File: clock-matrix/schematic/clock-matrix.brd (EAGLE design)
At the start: 30 x 50 mm, 80 parts, among them IC1 WS2811-SOP8, IC2 WS2811-SOP8, IC3 74HC595D, U1 Tiny45-20-SMT, X2 USB-MICROB

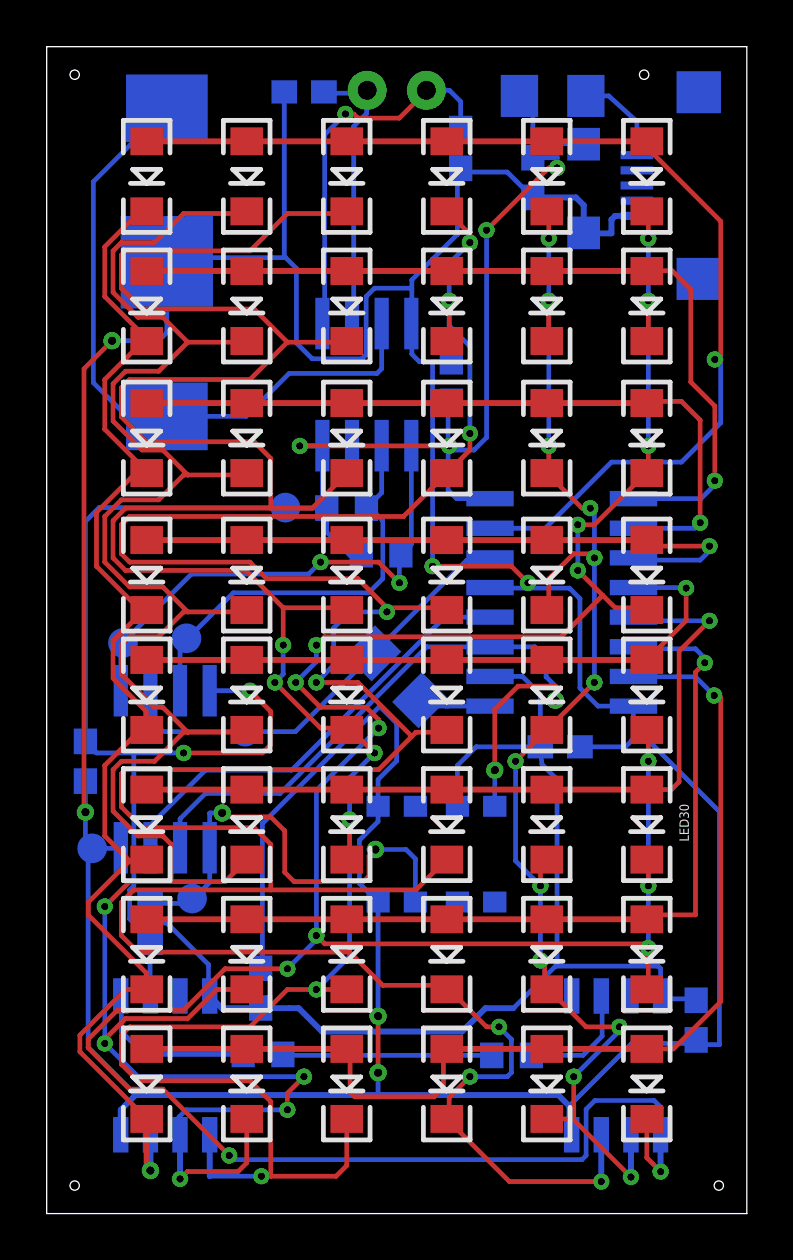
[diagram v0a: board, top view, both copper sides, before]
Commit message: Relocated files, removed unused files, updated christmas and clock board and other changes
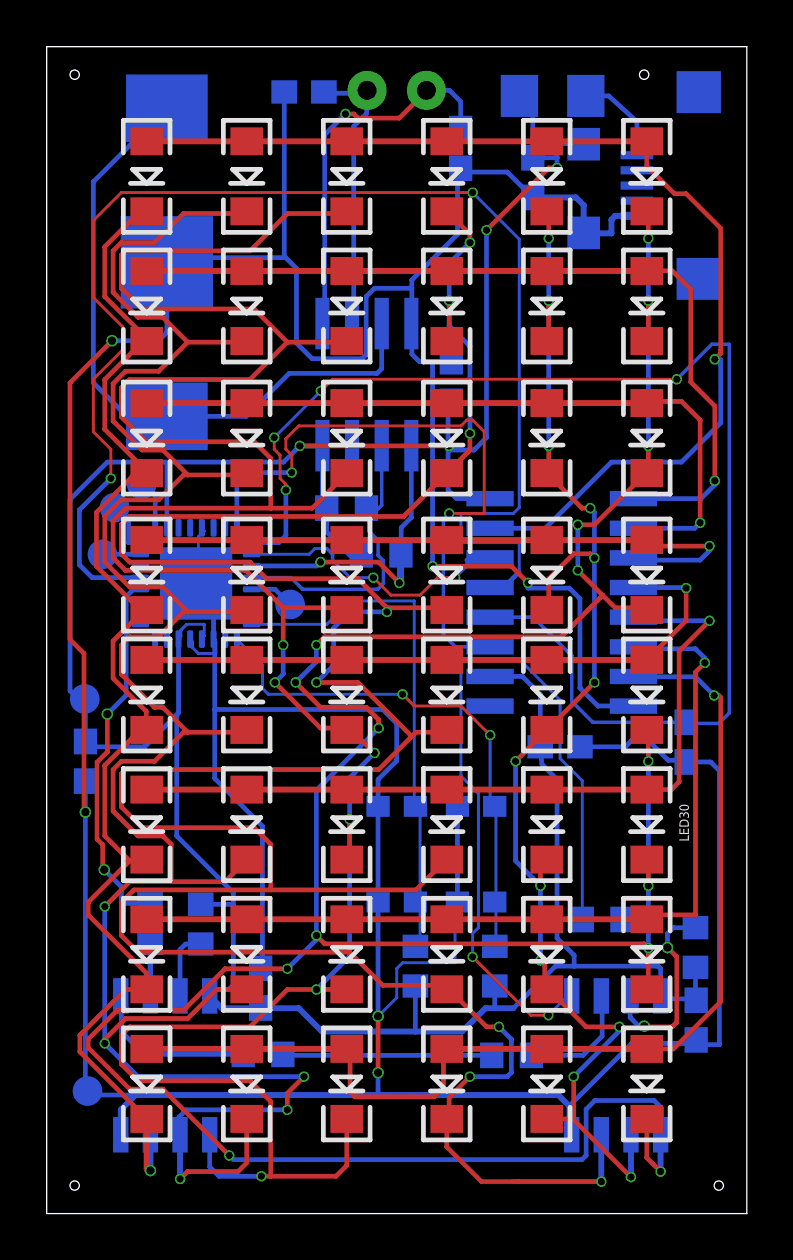
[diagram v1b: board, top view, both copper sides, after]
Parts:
- removed U1: Tiny45-20-SMT, SparkFun-Retired:SO08-EIAJ_MCU
- added C6: (no value), rcl:C0603
- added R2, R4, R7, R8: 33, adafruit:R0603
- added U2: ATMEGA328P-MU, Microcontroller:VQFN-32
- R3: value 0 -> 33; device audio amplifier example:R1206 -> adafruit:R0603
- moved TP1 13.3 mm to (10.4, 26.1)
- moved R3 13.1 mm to (19.2, 10.6), turned to 270 degrees
- moved TP6 11.9 mm to (1.63, 22.1)
- moved TP2 11.1 mm to (2.91, 30.2)
- moved TP5 10.4 mm to (1.75, 5.25)
- moved TP4 6.85 mm to (4.07, 31.2)
- moved TP3 5.09 mm to (2.39, 28.2)
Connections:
- removed net CLK: IC3.11, S1.1, S1.2, U1.2
- removed net RCK: IC3.12, U1.3
- new net AREF: U2.20
- new net BT0: R2.1, S2.1, S2.2, U2.32
- new net BT1: R3.1, S1.1, S1.2, U2.1
- new net LATCH: C6.1, IC3.12, U2.25
- new net LEDDATA: R9.1, U2.12
- new net MISO: TP2.TP, U2.16
- new net MOSI: TP3.TP, U2.15
- new net N$13: IC2.7, R8.2
- new net N$4: IC1.7, R7.2
- new net N$6: U2.8
- new net N$8: U2.7
- new net PWM: IC3.13, U2.13
- new net RCLK: IC3.11, U2.24
- new net RX: U2.30
- new net SCK: TP4.TP, U2.17
- new net TX: U2.31
- net 5V: now also R2.2, R3.2, R7.1, R8.1, U2.18, U2.4, U2.6; no longer S1.3, S1.4, U1.8
- net GND: now also C6.2, S1.3, S1.4, U2.21, U2.3, U2.33, U2.5; no longer IC3.13, U1.4
- net N$5: now also IC2.5, R4.2; no longer IC3.9, R3.1
- net RES: now also U2.29; no longer R9.1, S2.1, S2.2, U1.1
- net SCL: now also U2.28; no longer TP3.TP, U1.7
- net SDA: now also U2.27; no longer TP4.TP, U1.5
- net SER: now also U2.26; no longer R3.2, TP2.TP, U1.6
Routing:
- net PWM: track 0.00 -> 59.7 mm, vias 0 -> 2
- net LATCH: track 0.00 -> 56.4 mm, vias 0 -> 4
- net N$5: track 3.09 -> 33.5 mm, vias 0 -> 2
- net CLK: track 29.9 -> 0.00 mm, vias 2 -> 0
- net RCLK: track 0.00 -> 27.6 mm, vias 0 -> 2
- net GND: track 191.9 -> 217.5 mm
- net BT0: track 0.00 -> 22.7 mm
- net BT1: track 0.00 -> 22.4 mm, vias 0 -> 2
- net RCK: track 19.2 -> 0.00 mm
- net RES: track 20.5 -> 1.91 mm, vias 2 -> 0
- net LEDDATA: track 0.00 -> 16.0 mm, vias 0 -> 2
- net N$13: track 0.00 -> 8.46 mm, vias 0 -> 2
- net SDA: track 22.0 -> 14.4 mm
- net SER: track 20.5 -> 13.1 mm, vias 0 -> 2
- net SCL: track 18.3 -> 13.3 mm
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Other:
- board text removed: "G"
- board text removed: "MI"
- board text removed: "MO"
- board text removed: "R"
- board text removed: "SK"

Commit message: Minor board fixes and other changes
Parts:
- moved R15 0.20 mm to (12.8, 30.4)
- moved TP6 0.20 mm to (1.63, 22.2)
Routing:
- net SDA: track 14.4 -> 13.3 mm
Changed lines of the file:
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@@
 <drawing>
 <settings>
-<setting alwaysvectorfont="no"/>
+<setting alwaysvectorfont="yes"/>
 <setting verticaltext="up"/>
 </settings>
@@
 </class>
 </classes>
-<designrules name="jlcpcb-2layers">
+<designrules name="jlcpcb-2layers *">
 <description language="en">&lt;b&gt;JLCPCB design rules (2 layers)&lt;/b&gt;
 &lt;ul&gt;
@@
 <param name="mlMinCreamFrame" value="0mil"/>
 <param name="mlMaxCreamFrame" value="0mil"/>
-<param name="mlViaStopLimit" value="0mil"/>
+<param name="mlViaStopLimit" value="14mil"/>
 <param name="srRoundness" value="0"/>
 <param name="srMinRoundness" value="0mil"/>
@@
 <attribute name="NAME" x="12.695" y="27.195" size="1.27" layer="26" rot="MR180"/>
 </element>
-<element name="R15" library="rcl" package="R0603" value="10K" x="12.85" y="30.23" smashed="yes" rot="MR180">
-<attribute name="NAME" x="14.415" y="30.795" size="1.27" layer="26" rot="MR180"/>
+<element name="R15" library="rcl" package="R0603" value="10K" x="12.85" y="30.43" smashed="yes" rot="MR180">
+<attribute name="NAME" x="14.415" y="30.995" size="1.27" layer="26" rot="MR180"/>
 </element>
 <element name="R6" library="adafruit" package="R0603" value="33" x="19.92" y="6.78" smashed="yes" rot="MR180">
@@
 <attribute name="VALUE" x="2.385" y="4.488" size="0.0254" layer="28" rot="MR0"/>
 </element>
-<element name="TP6" library="testpad" package="B1,27" value="TPB1,27" x="1.63" y="22.05" smashed="yes" rot="MR0">
-<attribute name="TP_SIGNAL_NAME" value="" x="2.265" y="20.145" size="1" layer="38" rot="MR0"/>
-<attribute name="VALUE" x="2.265" y="21.288" size="0.0254" layer="28" rot="MR0"/>
-<attribute name="VALUE" x="2.265" y="21.288" size="0.0254" layer="28" rot="MR0"/>
+<element name="TP6" library="testpad" package="B1,27" value="TPB1,27" x="1.63" y="22.25" smashed="yes" rot="MR0">
+<attribute name="TP_SIGNAL_NAME" value="" x="2.265" y="20.345" size="1" layer="38" rot="MR0"/>
+<attribute name="VALUE" x="2.265" y="21.488" size="0.0254" layer="28" rot="MR0"/>
+<attribute name="VALUE" x="2.265" y="21.488" size="0.0254" layer="28" rot="MR0"/>
 </element>
 <element name="U$2" library="SparkFun" package="SO08" value="DS1307SO8" x="13.72" y="35.52" smashed="yes" rot="MR180">
@@
 <wire x1="14.2" y1="18.6" x2="15" y2="19.4" width="0.2032" layer="16"/>
 <wire x1="22.85" y1="22.51589375" x2="23.616075" y2="21.74981875" width="0.2032" layer="16"/>
-<wire x1="23.62089375" y1="21.745" x2="23.616075" y2="21.74981875" width="0.2032" layer="16"/>
 <wire x1="22.85" y1="22.51589375" x2="22.85" y2="26.35" width="0.2032" layer="16"/>
 <wire x1="14.075" y1="13.475" x2="14.2" y2="13.35" width="0.2032" layer="16"/>
@@
 <wire x1="1.6" y1="17.2" x2="1.66" y2="17.2" width="0.2032" layer="1"/>
 <via x="1.66" y="17.2" extent="1-16" drill="0.35"/>
-<wire x1="1.6" y1="17.2" x2="1.6" y2="24" width="0.2032" layer="1"/>
+<wire x1="1.6" y1="17.2" x2="1.6" y2="22.2" width="0.2032" layer="1"/>
+<wire x1="1.6" y1="22.2" x2="1.6" y2="24" width="0.2032" layer="1"/>
 <wire x1="14.2" y1="8.4576" x2="14.2" y2="8.4" width="0.2032" layer="16"/>
 <via x="14.2" y="8.4576" extent="1-16" drill="0.35"/>
@@
 <contactref element="LED13" pad="C"/>
 <wire x1="4.445" y1="3.3766" x2="4.445" y2="1.845" width="0.254" layer="16"/>
-<wire x1="4.445" y1="1.845" x2="4.4" y2="1.8" width="0.254" layer="16"/>
 <wire x1="4.285709375" y1="4.0555" x2="4.285709375" y2="1.914290625" width="0.254" layer="1"/>
 <wire x1="4.285709375" y1="1.914290625" x2="4.4" y2="1.8" width="0.254" layer="1"/>
@@
 <wire x1="14.224" y1="27.9146" x2="11.7348" y2="27.9146" width="0.2032" layer="1"/>
 <wire x1="15.113" y1="27.0256" x2="14.224" y2="27.9146" width="0.2032" layer="1"/>
-<wire x1="15.113" y1="28.0924" x2="15.113" y2="27.0256" width="0.2032" layer="16"/>
 <via x="11.7348" y="27.9146" extent="1-16" drill="0.3048"/>
 <via x="15.113" y="27.0256" extent="1-16" drill="0.3048"/>
@@
 <contactref element="U2" pad="28"/>
 <contactref element="R15" pad="2"/>
-<wire x1="13.75" y1="30" x2="14" y2="30" width="0.127" layer="16"/>
+<wire x1="13.793478125" y1="30" x2="13.8" y2="30" width="0.127" layer="16"/>
+<wire x1="13.8" y1="30" x2="14" y2="30" width="0.127" layer="16"/>
 <wire x1="14" y1="30" x2="14.0472" y2="30.0472" width="0.127" layer="16"/>
-<wire x1="13.75" y1="30" x2="13.7" y2="30.23" width="0.127" layer="16"/>
+<wire x1="13.793478125" y1="30" x2="13.7" y2="30.43" width="0.127" layer="16"/>
 <wire x1="8.8" y1="27.25" x2="8.785" y2="27.25" width="0.127" layer="16"/>
 <wire x1="14.25" y1="32.75" x2="14.355" y2="32.9038" width="0.127" layer="16"/>
-<wire x1="14.355" y1="32.9038" x2="14.355" y2="30.355" width="0.1524" layer="16"/>
-<wire x1="14.355" y1="30.355" x2="14" y2="30" width="0.1524" layer="16"/>
-<wire x1="13.7" y1="30.23" x2="13.8" y2="30.13" width="0.1524" layer="16"/>
+<wire x1="14.355" y1="32.9038" x2="14.355" y2="30.555" width="0.1524" layer="16"/>
+<wire x1="14.355" y1="30.555" x2="13.8" y2="30" width="0.1524" layer="16"/>
+<wire x1="13.7" y1="30.43" x2="13.8" y2="30.33" width="0.1524" layer="16"/>
 <wire x1="14.2" y1="28.2" x2="14.2" y2="28.84736875" width="0.1524" layer="16"/>
 <wire x1="13.8" y1="29.24736875" x2="14.2" y2="28.84736875" width="0.1524" layer="16"/>
-<wire x1="13.8" y1="30.13" x2="13.8" y2="29.24736875" width="0.1524" layer="16"/>
+<wire x1="13.8" y1="30.33" x2="13.8" y2="29.24736875" width="0.1524" layer="16"/>
 <wire x1="14.4294" y1="27.9706" x2="14.4294" y2="27" width="0.1524" layer="16"/>
 <wire x1="14.4294" y1="27.9706" x2="14.2" y2="28.2" width="0.1524" layer="16"/>
@@
 <wire x1="19.2" y1="8.8" x2="20" y2="8.8" width="0.254" layer="16"/>
 <wire x1="26.305" y1="9.3234" x2="26.305" y2="9.2" width="0.254" layer="16"/>
-<wire x1="12" y1="29.2" x2="12" y2="30.23" width="0.2032" layer="16"/>
+<wire x1="12" y1="29.2" x2="12" y2="30.43" width="0.2032" layer="16"/>
 <wire x1="12" y1="29.2" x2="13" y2="28.2" width="0.2032" layer="16"/>
 <wire x1="13" y1="28.2" x2="13.45" y2="28.2" width="0.2032" layer="16"/>
 <wire x1="13.45" y1="28.2" x2="13.48" y2="28.23" width="0.2032" layer="16"/>
-<wire x1="11.815" y1="32.9038" x2="11.815" y2="30.415" width="0.2032" layer="16"/>
-<wire x1="11.815" y1="30.415" x2="12" y2="30.23" width="0.2032" layer="16"/>
+<wire x1="11.815" y1="32.9038" x2="11.815" y2="30.615" width="0.2032" layer="16"/>
+<wire x1="11.815" y1="30.615" x2="12" y2="30.43" width="0.2032" layer="16"/>
 <contactref element="IC3" pad="16"/>
 <contactref element="IC3" pad="10"/>
@@
 <wire x1="9.2456" y1="8.89" x2="9.17" y2="8.81" width="0.2032" layer="16"/>
 <wire x1="9.2456" y1="8.89" x2="9.2456" y2="8.8" width="0.2032" layer="16"/>
-<wire x1="21.8694" y1="18.6024" x2="21.8694" y2="14.4" width="0.2032" layer="16"/>
-<wire x1="21.8694" y1="14.4" x2="21.8694" y2="11.8" width="0.2032" layer="16"/>
+<wire x1="21.8694" y1="18.6024" x2="21.8694" y2="11.8" width="0.2032" layer="16"/>
 <wire x1="21.2211125" y1="19.2506875" x2="21.8694" y2="18.6024" width="0.2032" layer="16"/>
 <wire x1="21.2211125" y1="19.2506875" x2="21.150446875" y2="19.995296875" width="0.2032" layer="16"/>
@@
 <wire x1="5.15" y1="32.1" x2="5.25" y2="32.2" width="0.2032" layer="16"/>
 <wire x1="5.65" y1="24.615" x2="5.65" y2="21.45" width="0.2032" layer="16"/>
-<wire x1="5.575" y1="21.375" x2="5.5" y2="21.3" width="0.2032" layer="16"/>
-<wire x1="5.5" y1="21.3" x2="4.2" y2="20" width="0.2032" layer="16"/>
+<wire x1="5.575" y1="21.375" x2="4.2" y2="20" width="0.2032" layer="16"/>
 <wire x1="1.88655625" y1="20" x2="4.2" y2="20" width="0.2032" layer="16"/>
 <wire x1="1.88655625" y1="20" x2="1.6622125" y2="20.22434375" width="0.2032" layer="16"/>
 <wire x1="1.88655625" y1="20" x2="1.84524375" y2="20" width="0.2032" layer="16"/>
 <wire x1="1.84524375" y1="20" x2="1.68876875" y2="20.156475" width="0.2032" layer="16"/>
-<wire x1="1.66" y1="22.02" x2="1.66" y2="20.23" width="0.2032" layer="16"/>
+<wire x1="1.66" y1="22.02" x2="1.66" y2="21.8" width="0.2032" layer="16"/>
+<wire x1="1.66" y1="21.8" x2="1.66" y2="20.23" width="0.2032" layer="16"/>
 <wire x1="6.985" y1="9.6" x2="6.985" y2="9.3234" width="0.2032" layer="16"/>
 <wire x1="5.575" y1="21.375" x2="5.575" y2="16.175" width="0.2032" layer="16"/>
 <wire x1="5.575" y1="21.375" x2="5.65" y2="21.45" width="0.2032" layer="16"/>
 <wire x1="1" y1="30.6" x2="1" y2="22.4" width="0.2032" layer="16"/>
-<wire x1="1" y1="22.4" x2="1.35" y2="22.05" width="0.2032" layer="16"/>
-<wire x1="1.35" y1="22.05" x2="1.63" y2="22.05" width="0.2032" layer="16"/>
+<wire x1="1" y1="22.4" x2="1.15" y2="22.25" width="0.2032" layer="16"/>
+<wire x1="1.15" y1="22.25" x2="1.63" y2="22.25" width="0.2032" layer="16"/>
 <contactref element="R7" pad="1"/>
 <contactref element="R8" pad="1"/>
@@
 <wire x1="27.8" y1="10.55" x2="27.8" y2="9.23" width="0.2032" layer="16"/>
 <wire x1="27.8" y1="9.23" x2="27.77" y2="9.2" width="0.2032" layer="16"/>
-<wire x1="1.66" y1="22.02" x2="1.63" y2="22.05" width="0" layer="19" extent="16-16"/>
+<wire x1="1.63" y1="22.25" x2="1.66" y2="22.22" width="0.1524" layer="16"/>
+<wire x1="1.66" y1="22.22" x2="1.66" y2="21.8" width="0.1524" layer="16"/>
 </signal>
 <signal name="SER">
@@
 <wire x1="24.2" y1="32.2" x2="27.2" y2="32.2" width="0.2032" layer="16"/>
 <wire x1="28.8824" y1="33.8824" x2="28.8824" y2="36.4" width="0.2032" layer="16"/>
-<wire x1="28.8824" y1="36.4" x2="28.8824" y2="36.6" width="0.2032" layer="16"/>
 <wire x1="27.2" y1="32.2" x2="28.8824" y2="33.8824" width="0.2032" layer="16"/>
 <wire x1="28.8824" y1="36.4" x2="28.6824" y2="36.6" width="0.2032" layer="16"/>
@@
 <wire x1="25.714259375" y1="44.885740625" x2="26.9" y2="43.7" width="0.2" layer="1"/>
 <wire x1="27.4" y1="43.7" x2="28.8824" y2="42.2176" width="0.2" layer="1"/>
-<wire x1="28.8824" y1="42.2176" x2="28.8824" y2="37" width="0.2" layer="1"/>
-<wire x1="28.8824" y1="37" x2="28.8824" y2="36.854" width="0.2" layer="1"/>
+<wire x1="28.8824" y1="42.2176" x2="28.8824" y2="36.854" width="0.2" layer="1"/>
 <wire x1="28.8824" y1="36.854" x2="28.6284" y2="36.6" width="0.2" layer="1"/>
 </signal>
